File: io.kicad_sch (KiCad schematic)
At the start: 107 parts, among them CN1 DF40C-50DP-0.4V, J1 USB3_A, J13 WiFi SMA, J14 BLE SMA, J15 WiFi PATCH, J16 BLE PATCH, J17 BLE PATCH, J18 WIFI PATCH, U1 FUSB302BMPX, U12 PI3USB302-AZBEX, U13 VL817-Q7, U14 SiP32508DT, U15 TS5A23157DGSR, U16 AMLGA7921, U17 SiP32508DT, U30 PE4259-63, U36 PE4259-63, U37 2450CF15A0100001E, U38 X4C60K1-20S, U39 XEC24P3-30G, U40 AD8317ACPZ-R7, U41 AD8317ACPZ-R7, U42 AD8317ACPZ-R7, U43 LM339D, U7 HD3SS3220RNHR, Y2 Crystal

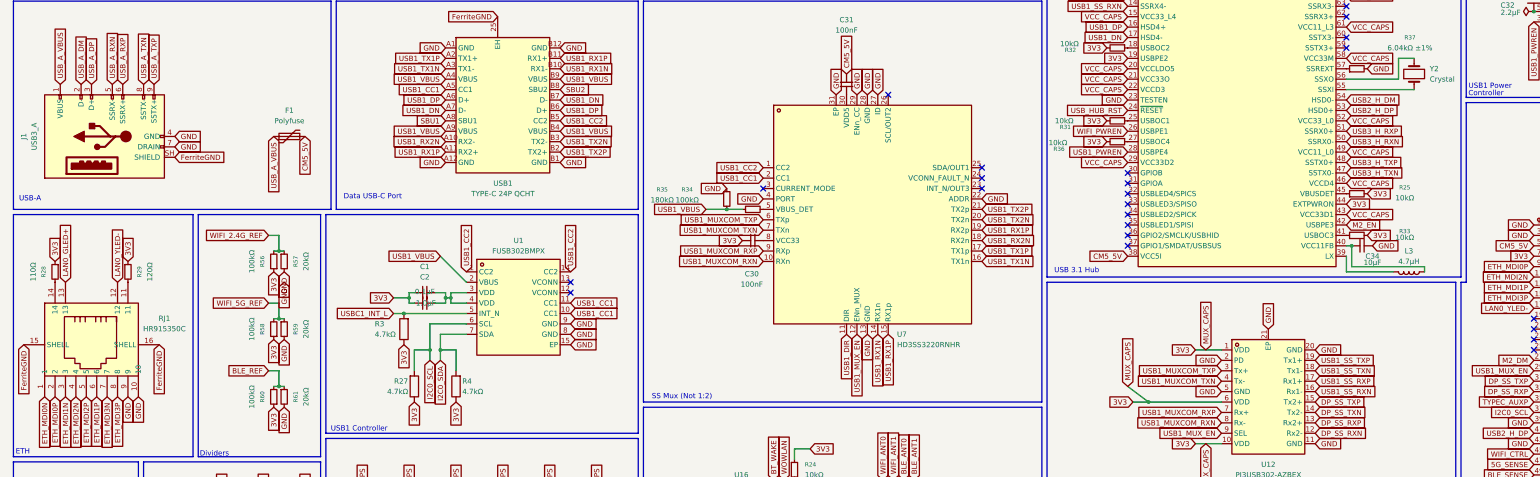
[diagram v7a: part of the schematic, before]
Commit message: finished slateconnect i2c gpio expander, completed led status bar schematic, fixed all drc errors, started assigning footprints and started bom
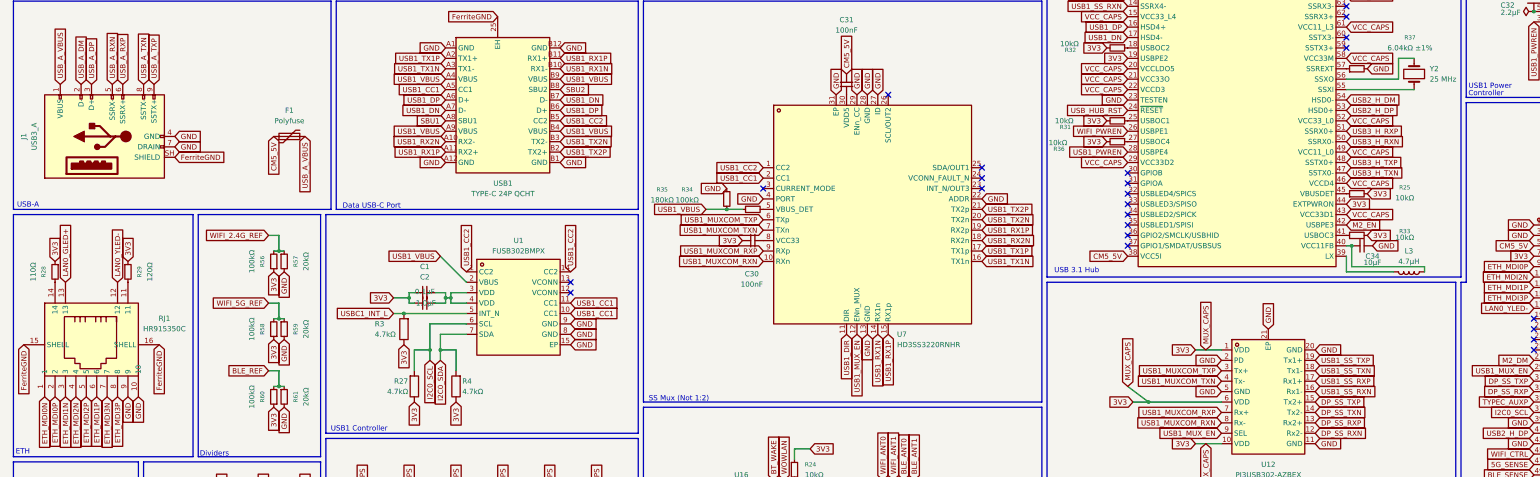
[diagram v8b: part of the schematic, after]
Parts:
- C1, C106, C108, C22, C23, C24, C26, C27, C30, C31, C33, C36, C37, C38, C39, C40, C41, C43, C44, C45, C46, C47, C48, C49, C50, C51, C52, C53, C54, C55, C56: footprint (none) -> Capacitor_SMD:C_0603_1608Metric; MPN (none) -> CL10B104KB8NNNC; Manufacturer (none) -> Samsung Electro-Mechanics
- C100, C105, C107, C99: footprint (none) -> Capacitor_SMD:C_0603_1608Metric; MPN (none) -> CL10C101JB8NNNC; Manufacturer (none) -> Samsung Electro-Mechanics
- C103: footprint (none) -> Capacitor_SMD:C_0603_1608Metric; MPN (none) -> CL10C829JB8NNNC; Manufacturer (none) -> Samsung Electro-Mechanics
- C2: footprint (none) -> Capacitor_SMD:C_0603_1608Metric; MPN (none) -> CL10B105KA8NNNC; Manufacturer (none) -> Samsung Electro-Mechanics
- C32, C42: footprint (none) -> Capacitor_SMD:C_0603_1608Metric; MPN (none) -> CL10B225KA8NNNC; Manufacturer (none) -> Samsung Electro-Mechanics
- C34: footprint (none) -> Capacitor_SMD:C_0603_1608Metric; MPN (none) -> CL10A106KP8NNNC; Manufacturer (none) -> Samsung Electro-Mechanics
- F1: footprint (none) -> Fuse:Fuse_1206_3216Metric; MPN (none) -> Littelfuse 1206L100/60YR; Manufacturer (none) -> DigiKey
- J13, J14: footprint (none) -> Connector_Coaxial:U.FL_Hirose_U.FL-R-SMT-1(10); MPN (none) -> Hirose U.FL-R-SMT-1(10); Manufacturer (none) -> DigiKey
- J15, J18: MPN (none) -> Molex 1461870200; Manufacturer (none) -> Molex
- J16, J17: MPN (none) -> Antenna Company AC11501-050UF; Manufacturer (none) -> Antenna Company
- L3: MPN (none) -> Bourns SRP5030CA-4R7M; Manufacturer (none) -> DigiKey
- R24, R25, R31, R32, R33, R36, R47, R50, R52, R53, R54, R55: footprint (none) -> Resistor_SMD:R_0603_1608Metric; MPN (none) -> RC0603FR-0710KL; Manufacturer (none) -> Yageo
- R27, R3, R4: footprint (none) -> Resistor_SMD:R_0603_1608Metric; MPN (none) -> RC0603FR-074K7L; Manufacturer (none) -> Yageo
- R28: footprint (none) -> Resistor_SMD:R_0603_1608Metric; MPN (none) -> RC0603FR-07110RL; Manufacturer (none) -> Yageo
- R29: footprint (none) -> Resistor_SMD:R_0603_1608Metric; MPN (none) -> RC0603FR-07120RL; Manufacturer (none) -> Yageo
- R34, R56, R58, R60: footprint (none) -> Resistor_SMD:R_0603_1608Metric; MPN (none) -> RC0603FR-07100KL; Manufacturer (none) -> Yageo
- R35: footprint (none) -> Resistor_SMD:R_0603_1608Metric; MPN (none) -> RC0603FR-07180KL; Manufacturer (none) -> Yageo
- R57, R59, R61: footprint (none) -> Resistor_SMD:R_0603_1608Metric; MPN (none) -> RC0603FR-0720KL; Manufacturer (none) -> Yageo
- U14, U17: MPN (none) -> SiP32508DT; Manufacturer (none) -> LCSC
- U16: MPN (none) -> AMLGA7921; Manufacturer (none) -> LCSC
- U37: MPN (none) -> 2450CF15A0100001E; Manufacturer (none) -> LCSC
- U38: MPN (none) -> X4C60K1-20S; Manufacturer (none) -> LCSC
- U39: MPN (none) -> XEC24P3-30G; Manufacturer (none) -> LCSC
- Y2: value Crystal -> 25 MHz; MPN (none) -> ECS-250-12-33Q-DS; Manufacturer (none) -> DigiKey
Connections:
- net CM5_5V: now also F1.1; no longer F1.2
- net USB_A_VBUS: now also F1.2; no longer F1.1
